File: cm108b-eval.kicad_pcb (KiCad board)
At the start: 2 copper layers, 60 x 50 mm, 42 parts, among them IC1 CM108B, J1 SPKR, J2 MIC, J3 RADIO_DATA, SW1 MUTE_REC, SW2 MUTE_PLAY, SW3 VOL_DN, SW4 VOL_UP

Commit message: Couple of silkscreen improvements
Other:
- board text added: "HI"
- board text added: "LO"
- board text added: "MIC SPK GND"
- board text removed: "GND SPK MIC"

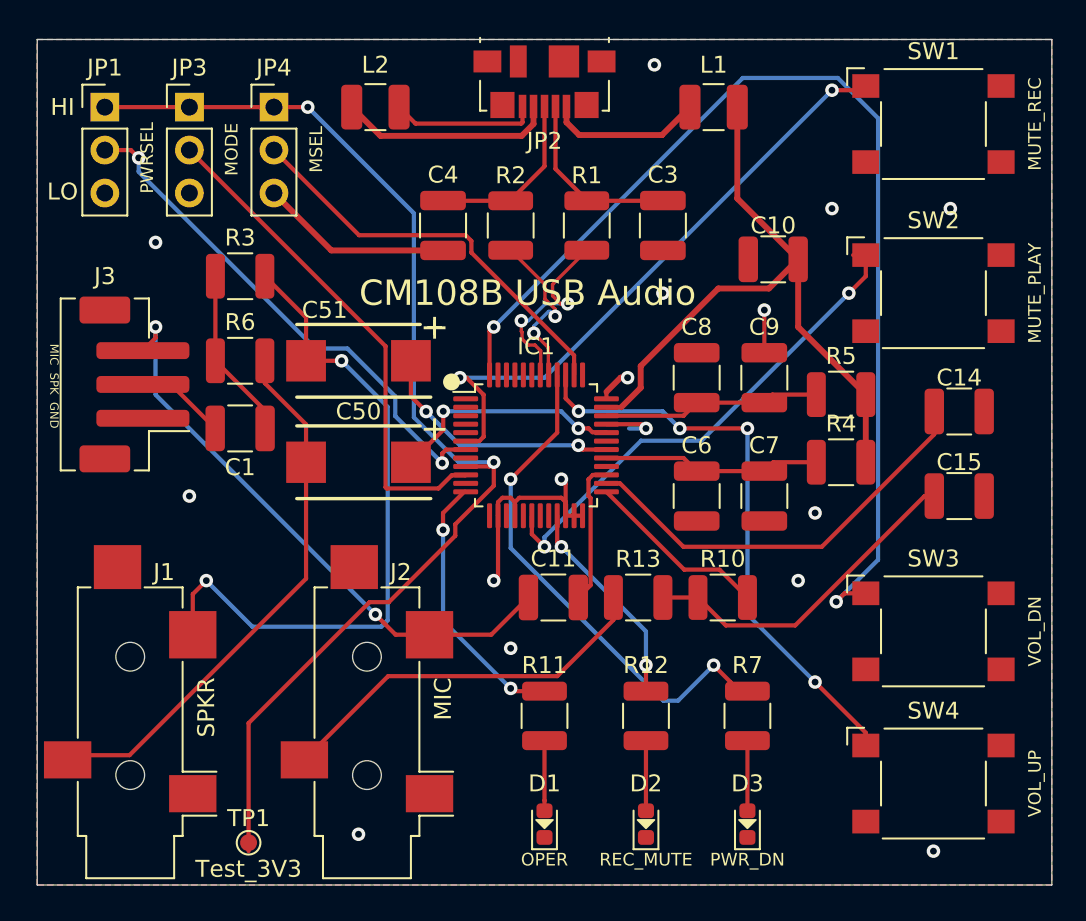
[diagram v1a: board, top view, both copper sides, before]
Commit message: Update micro USB part, and clean up libraries
The Molex micro USB is nearly impossible to hand solder, so I'm moving to the CUI
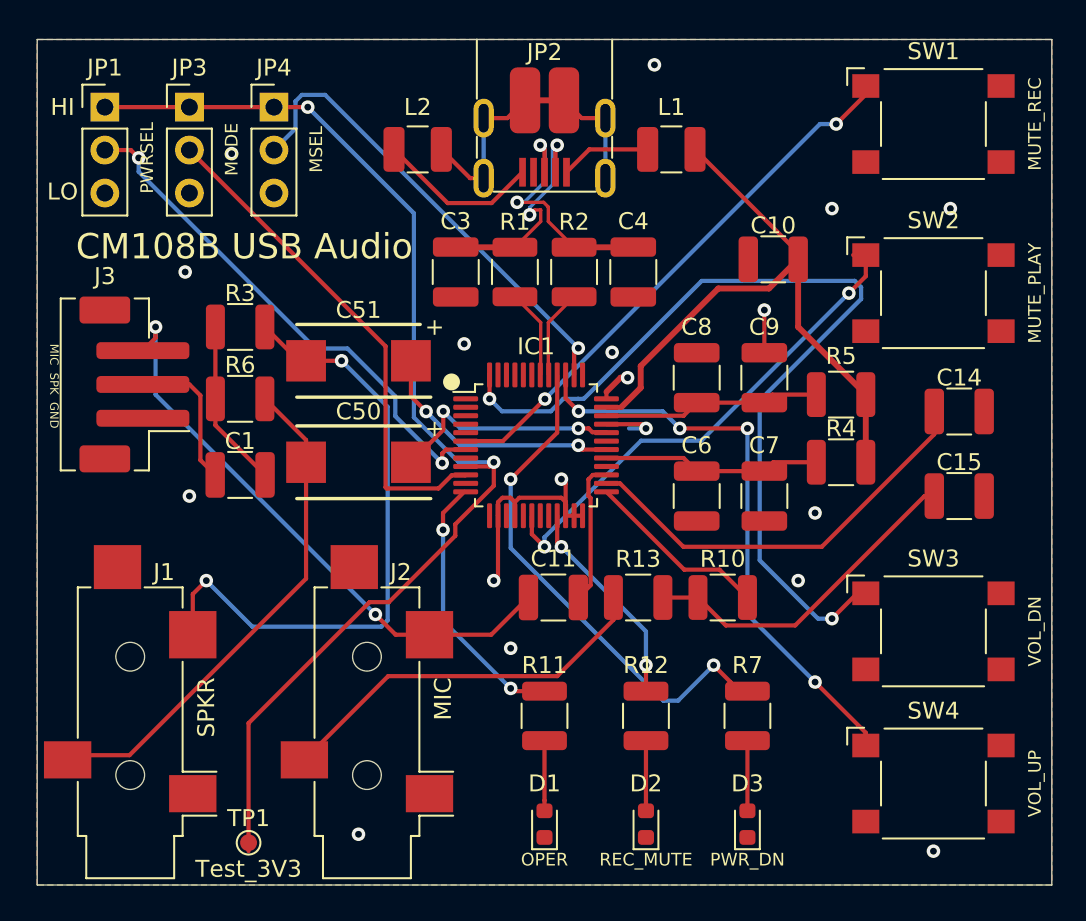
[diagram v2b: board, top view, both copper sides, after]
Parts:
- C50, C51: footprint 293D477X9010E2TE3:CAPPM7343X430N -> Vishay:CAPPM7343X430N
- JP2: footprint Connector_USB:USB_Micro-B_Molex_47346-0001 -> CUI:UJ2-MIBH-4-SMT
- moved C3 12.6 mm to (154.8, 83.8)
- moved C4 11.6 mm to (165.2, 83.8)
- moved R1 5.06 mm to (158.2, 83.8)
- moved R2 4.65 mm to (161.8, 83.8)
- moved L1 3.54 mm to (167.5, 76.5)
- moved L2 3.54 mm to (152.5, 76.5)
- moved R3 3.00 mm to (142.0, 87.0)
- moved C1 2.75 mm to (142.0, 95.8)
- moved JP2 2.50 mm to (160.0, 70.0), turned to 0 degrees
- moved R6 2.25 mm to (142.0, 91.2)
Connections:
- net Net-(C3-Pad1) renamed /USB-
- net Net-(C4-Pad1) renamed /USB+
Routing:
- net Net-(JP2-Pad6): track 0.00 -> 18.4 mm
- net GND: track 46.2 -> 31.7 mm, vias 16 -> 18
- net /VOLDN: track 64.6 -> 54.3 mm
- net Net-(JP2-Pad5): track 8.67 -> 0.00 mm
- net /D-: track 11.7 -> 5.27 mm, vias 2 -> 0
- net /D+: track 9.99 -> 5.27 mm, vias 2 -> 0
- net /USB+: track 10.4 -> 14.6 mm, vias 0 -> 2
- net /MUTER: track 36.6 -> 32.7 mm
- net Net-(JP2-Pad1): track 9.23 -> 5.36 mm
- net /MSEL: track 24.3 -> 28.2 mm, vias 0 -> 1
- net Net-(C1-Pad2): track 5.35 -> 8.73 mm
- net /AUDIO_R: track 40.6 -> 37.9 mm
- net /USB-: track 10.8 -> 13.5 mm, vias 0 -> 2
- net /AUDIO_L: track 32.8 -> 30.6 mm
- net VBUS: track 39.9 -> 38.4 mm
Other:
- board text added: "CM108B Audio Evaluation Board v4 C. Keller 2021-04-14"
- board text removed: "+"
- board text removed: "CM108B Audio Evaluation Board v3 C. Keller 2021-04-05"

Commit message: Add CC-BY-4.0 license
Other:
- board text added: "CM108B Audio Evaluation Board v4 C. Keller 2021-04-14 https://github.com/k0swe/cm108b-eval"
- board text removed: "CM108B Audio Evaluation Board v4 C. Keller 2021-04-14"
